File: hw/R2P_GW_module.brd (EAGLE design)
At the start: 40 x 60 mm, 70 parts, among them U1 STM32F407VG, U2 DP83848C, U3 LD3985XX, U4 MAX3051, X1 MICROMATCH-4, X2 47589-0001, X4 RJ45-43860, X5 RJ45-43860, X6 FTSH-105

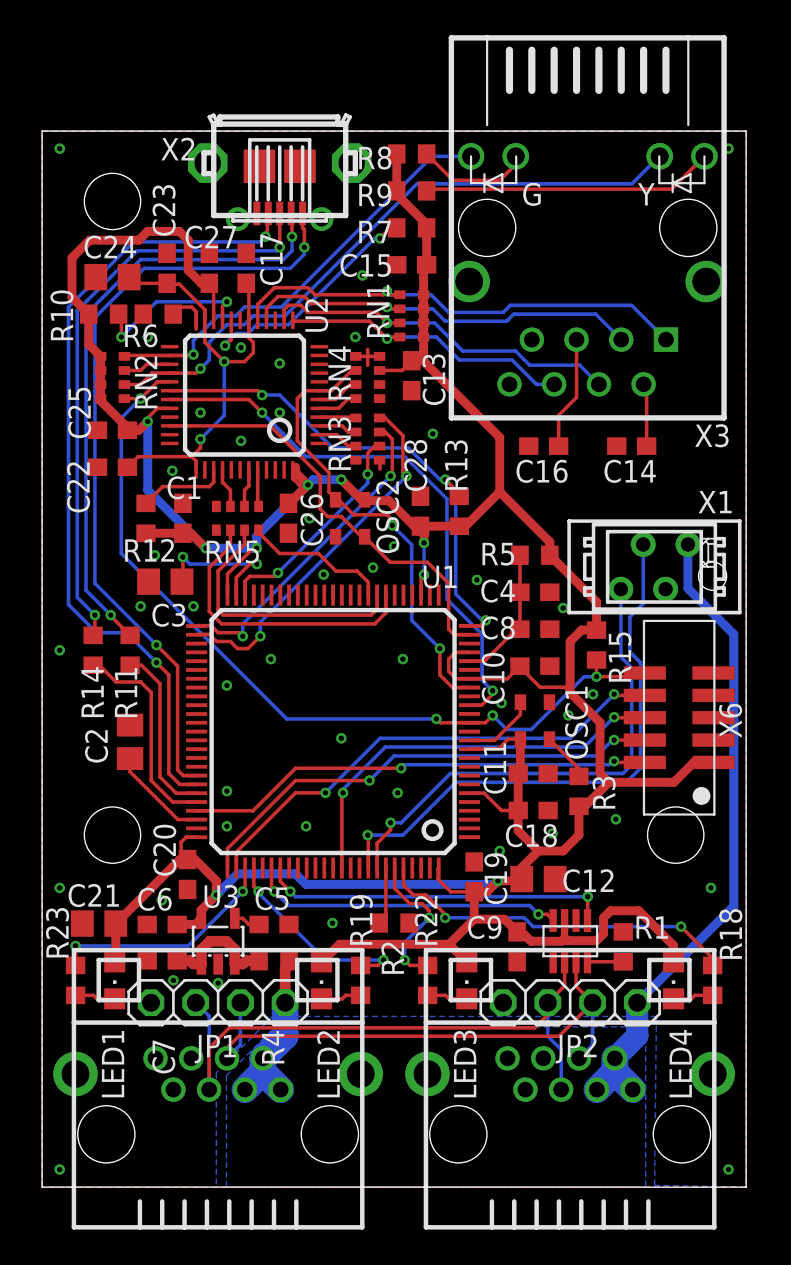
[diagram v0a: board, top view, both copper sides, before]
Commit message: Small fixes
Ethernet CT and CR wired to VDD.
R12 changed from 100k to 2k2.
Small changes in traces.

Andrea Zoppi
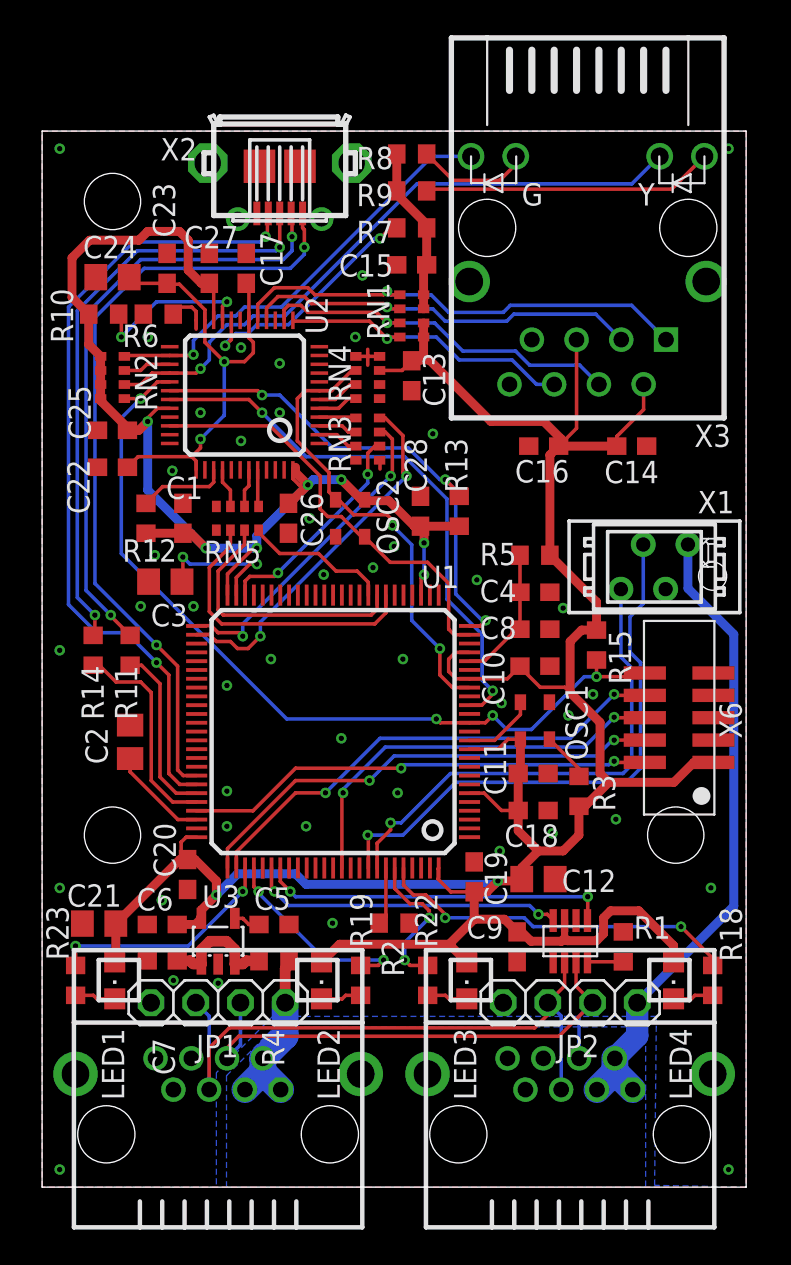
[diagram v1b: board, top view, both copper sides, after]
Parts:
- C11, C28: value 15p -> 10n
- turned C14 to 180 degrees
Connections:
- removed net N$13: C14.2, X3.2
- removed net N$16: C16.2, X3.5
- net +3V3: now also C14.2, C16.2, X3.2, X3.5
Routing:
- net +3V3: track 223.3 -> 235.9 mm
- net N$16: track 6.47 -> 0.00 mm
- net N$13: track 3.58 -> 0.00 mm

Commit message: Small updates
Andrea Zoppi
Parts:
- R12: value 100k -> 2k2
- moved C13 0.50 mm to (21.0, 45.6)
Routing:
- net +3V3: track 235.9 -> 241.6 mm
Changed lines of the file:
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@@
 <layer number="37" name="tTest" color="7" fill="1" visible="no" active="yes"/>
 <layer number="38" name="bTest" color="7" fill="1" visible="no" active="yes"/>
-<layer number="39" name="tKeepout" color="4" fill="11" visible="no" active="yes"/>
-<layer number="40" name="bKeepout" color="1" fill="11" visible="no" active="yes"/>
+<layer number="39" name="tKeepout" color="4" fill="11" visible="yes" active="yes"/>
+<layer number="40" name="bKeepout" color="1" fill="11" visible="yes" active="yes"/>
 <layer number="41" name="tRestrict" color="4" fill="10" visible="no" active="yes"/>
 <layer number="42" name="bRestrict" color="1" fill="10" visible="no" active="yes"/>
@@
 <attribute name="OC_FARNELL" value="unknown" x="21" y="49.5" size="1.778" layer="27" rot="R270" display="off"/>
 </element>
-<element name="C13" library="rcl" package="C0603" value="100n" x="21" y="46.1" smashed="yes" rot="R270">
-<attribute name="NAME" x="21.635" y="47.435" size="1.27" layer="25" rot="R270"/>
-<attribute name="VALUE" x="19.095" y="46.735" size="1.27" layer="27" rot="R270"/>
+<element name="C13" library="rcl" package="C0603" value="100n" x="21" y="45.6" smashed="yes" rot="R270">
+<attribute name="NAME" x="21.635" y="46.935" size="1.27" layer="25" rot="R270"/>
+<attribute name="VALUE" x="19.095" y="46.235" size="1.27" layer="27" rot="R270"/>
 </element>
 <element name="C14" library="rcl" package="C0603" value="100n" x="33.5" y="42.1" smashed="yes" rot="R180">
@@
 <attribute name="VALUE" x="17.23" y="44.095" size="1.27" layer="27" ratio="10" rot="R90"/>
 </element>
-<element name="R12" library="rcl" package="R0603" value="100k" x="5.9" y="38" smashed="yes" rot="R270">
+<element name="R12" library="rcl" package="R0603" value="2k2" x="5.9" y="38" smashed="yes" rot="R270">
 <attribute name="NAME" x="4.565" y="35.535" size="1.27" layer="25"/>
 <attribute name="VALUE" x="3.995" y="38.635" size="1.27" layer="27" rot="R270"/>
@@
 <wire x1="28.3" y1="28.4" x2="29.7" y2="28.4" width="0.2032" layer="1"/>
 <wire x1="29.7" y1="28.4" x2="30" y2="28.1" width="0.2032" layer="1"/>
-<wire x1="20.45" y1="46.4" x2="19.175" y2="46.4" width="0.2032" layer="1"/>
 <wire x1="9.9" y1="16.6" x2="9.05125" y2="15.75125" width="0.508" layer="1"/>
 <wire x1="9.05125" y1="15.75125" x2="9.05125" y2="15.27" width="0.508" layer="1"/>
@@
 <wire x1="21.675" y1="50.7" x2="21.675" y2="52.225" width="0.508" layer="1"/>
 <wire x1="21.675" y1="52.225" x2="21.85" y2="52.4" width="0.508" layer="1"/>
-<wire x1="21.675" y1="48.3" x2="21.675" y2="47.175" width="0.508" layer="1"/>
-<wire x1="20.45" y1="46.4" x2="21" y2="46.95" width="0.2032" layer="1"/>
-<wire x1="28.85" y1="35.9" x2="28.85" y2="41.6" width="0.508" layer="1"/>
+<wire x1="28.85" y1="38.3" x2="28.85" y2="41.6" width="0.508" layer="1"/>
 <wire x1="28.85" y1="41.6" x2="29.35" y2="42.1" width="0.508" layer="1"/>
 <wire x1="32.65" y1="42.1" x2="29.35" y2="42.1" width="0.508" layer="1"/>
@@
 <wire x1="32.65" y1="42.65" x2="34.175" y2="44.175" width="0.2032" layer="1"/>
 <wire x1="34.175" y1="45.61" x2="34.175" y2="44.175" width="0.2032" layer="1"/>
-<wire x1="21.675" y1="47.175" x2="21.5" y2="47" width="0.508" layer="1"/>
-<wire x1="21.5" y1="47" x2="21.05" y2="47" width="0.508" layer="1"/>
-<wire x1="21.05" y1="47" x2="21" y2="46.95" width="0.508" layer="1"/>
-<wire x1="21.5" y1="47" x2="22" y2="47" width="0.508" layer="1"/>
-<wire x1="22" y1="47" x2="25.5" y2="43.5" width="0.508" layer="1"/>
-<wire x1="25.5" y1="43.5" x2="28.5" y2="43.5" width="0.508" layer="1"/>
+<wire x1="25.3" y1="43.5" x2="28.5" y2="43.5" width="0.508" layer="1"/>
 <wire x1="30.365" y1="43.115" x2="29.35" y2="42.1" width="0.2032" layer="1"/>
 <wire x1="28.5" y1="43.5" x2="29.5" y2="42.5" width="0.508" layer="1"/>
 <wire x1="29.5" y1="42.5" x2="29.5" y2="42.25" width="0.508" layer="1"/>
 <wire x1="29.5" y1="42.25" x2="29.35" y2="42.1" width="0.508" layer="1"/>
-<wire x1="21.675" y1="49.1" x2="21.675" y2="49.9" width="0" layer="19" extent="1-1"/>
-<wire x1="21.532040625" y1="33.634134375" x2="23.483159375" y2="30.383159375" width="0" layer="19" extent="1-1"/>
-<wire x1="14" y1="38.85" x2="14" y2="39.1" width="0" layer="19" extent="1-1"/>
+<wire x1="21.675" y1="49.9" x2="21.675" y2="49.1" width="0.508" layer="1"/>
+<wire x1="21.675" y1="48.3" x2="21.675" y2="47.125" width="0.508" layer="1"/>
+<wire x1="21.675" y1="47.125" x2="21" y2="46.45" width="0.508" layer="1"/>
+<wire x1="25.3" y1="43.5" x2="21.675" y2="47.125" width="0.508" layer="1"/>
+<wire x1="19.175" y1="46.4" x2="20.95" y2="46.4" width="0.2032" layer="1"/>
+<wire x1="20.95" y1="46.4" x2="21" y2="46.45" width="0.2032" layer="1"/>
+<wire x1="23.7" y1="37.55" x2="28.1" y2="37.55" width="0.508" layer="1"/>
+<wire x1="28.1" y1="37.55" x2="28.85" y2="38.3" width="0.508" layer="1"/>
+<wire x1="28.85" y1="35.9" x2="28.85" y2="36.8" width="0.508" layer="1"/>
+<wire x1="28.85" y1="36.8" x2="28.1" y2="37.55" width="0.508" layer="1"/>
+<wire x1="14" y1="39.1" x2="14" y2="38.85" width="0" layer="19" extent="1-1"/>
 </signal>
 <signal name="JTMS">
@@
 <wire x1="12" y1="48" x2="12" y2="47.4" width="0.2032" layer="1"/>
 <wire x1="12" y1="47.4" x2="11.5" y2="46.9" width="0.2032" layer="1"/>
-<wire x1="11.5" y1="46.9" x2="10.35" y2="46.9" width="0.2032" layer="1"/>
 <wire x1="10.35" y1="46.9" x2="9.25" y2="48" width="0.2032" layer="1"/>
 <via x="10.35" y="46.9" extent="1-16" drill="0.3" shape="octagon"/>
@@
 <wire x1="7.1" y1="51.35" x2="5.3" y2="51.35" width="0.2032" layer="1"/>
 <wire x1="5.3" y1="51.35" x2="4.95" y2="51.7" width="0.2032" layer="1"/>
+<wire x1="11.5" y1="46.9" x2="10.35" y2="46.9" width="0.2032" layer="1"/>
 </signal>
 <signal name="ETH_RMII_REF_CLK">
@@
 <wire x1="3" y1="31.45" x2="3" y2="32.5" width="0.2032" layer="1"/>
 </signal>
+<signal name="N$13">
+<via x="31" y="58.5" extent="1-16" drill="0.3" shape="octagon"/>
+</signal>
 </signals>

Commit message: Minor fixes
Andrea Zoppi
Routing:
- net GND: vias 44 -> 50
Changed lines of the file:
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@@
 <?xml version="1.0" encoding="utf-8"?>
 <!DOCTYPE eagle SYSTEM "eagle.dtd">
-<eagle version="6.3">
+<eagle version="6.4">
 <drawing>
 <settings>
@@
 <hole x="4" y="20" drill="3.2"/>
 <hole x="36" y="20" drill="3.2"/>
-<dimension x1="0" y1="0" x2="40" y2="0" x3="20" y3="-7.5" layer="47"/>
+<dimension x1="0" y1="0" x2="40" y2="0" x3="20" y3="-7.5" textsize="3.5" layer="47"/>
 <hole x="4" y="56" drill="3.2"/>
-<dimension x1="40" y1="0" x2="40" y2="40" x3="45" y3="20" layer="47"/>
-<dimension x1="40" y1="0" x2="40" y2="60" x3="50" y3="30" layer="47"/>
+<dimension x1="40" y1="0" x2="40" y2="40" x3="45" y3="20" textsize="3.5" layer="47"/>
+<dimension x1="40" y1="0" x2="40" y2="60" x3="50" y3="30" textsize="3.5" layer="47"/>
 </plain>
 <attributes>
@@
 <via x="20.5" y="30" extent="1-16" drill="0.3" shape="octagon"/>
 <via x="6" y="48.3" extent="1-16" drill="0.3" shape="octagon"/>
+<via x="31" y="58.5" extent="1-16" drill="0.3" shape="octagon"/>
+<via x="27.5" y="39.5" extent="1-16" drill="0.3" shape="octagon"/>
+<via x="30.5" y="39.5" extent="1-16" drill="0.3" shape="octagon"/>
+<via x="22.5" y="20" extent="1-16" drill="0.3" shape="octagon"/>
+<via x="11.3" y="44" extent="1-16" drill="0.3" shape="octagon"/>
+<via x="11.3" y="46.1" extent="1-16" drill="0.3" shape="octagon"/>
 </signal>
 <signal name="+3V3">
@@
 <wire x1="3" y1="31.45" x2="3" y2="32.5" width="0.2032" layer="1"/>
 </signal>
-<signal name="N$13">
-<via x="31" y="58.5" extent="1-16" drill="0.3" shape="octagon"/>
-</signal>
 </signals>
